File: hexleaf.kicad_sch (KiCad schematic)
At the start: 42 parts, among them IC1 ESP32-C3-FH4, J2 Conn_01x04, J5 Conn_01x08, J6 Conn_01x04, J7 Conn_01x08, SW1 SW_SPST, SW2 SW_SPST, Y1 ECS-400-10-37B2-CKM-TR

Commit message: added buck
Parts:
- added C? (x3): 22uF/16V, Resistor_SMD:R_0603_1608Metric, symbol Device:C_Small
- added C? (x2): 100n/50V, Resistor_SMD:R_0603_1608Metric, symbol Device:C_Small
- added L?: 33uH, hexleaf:CYH127, symbol Device:L_Small
- added R?: 24k, Resistor_SMD:R_0603_1608Metric, symbol Device:R_Small
- added R?: 75k, Resistor_SMD:R_0603_1608Metric, symbol Device:R_Small
- added R?: 100k, Resistor_SMD:R_0603_1608Metric, symbol Device:R_Small
- added R?: 0R, Resistor_SMD:R_0603_1608Metric, symbol Device:R_Small
- added U?: ZTP7193MA, Package_TO_SOT_SMD:SOT-23-8, symbol hexleaf:ZTP7193MA
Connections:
- net +3V3: now also C?.1, C?.1, L?.2, R?.2
- net GND: now also C?.2, C?.2, C?.2, C?.2, R?.1, U?.4 (GND)
- net VIN: now also C?.1, R?.1, U?.2 (VIN)
- new net: C?.1, L?.1, U?.3 (SW)
- new net: C?.2, U?.5 (BOOT)
- new net: R?.2, U?.6 (EN/SYNC)
- new net: C?.1, U?.7 (VCC)
- new net: R?.2, U?.8 (FB)
- new net: R?.1, R?.1, R?.2
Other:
- note added: "?"
- moved on the sheet: C1, C10, C2, C4, C5, C7, C9, L1

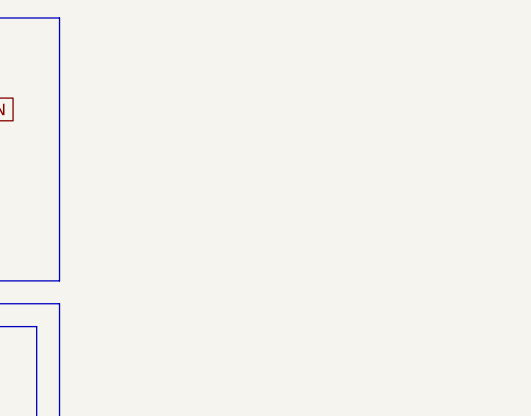
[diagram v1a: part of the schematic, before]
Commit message: added crystal
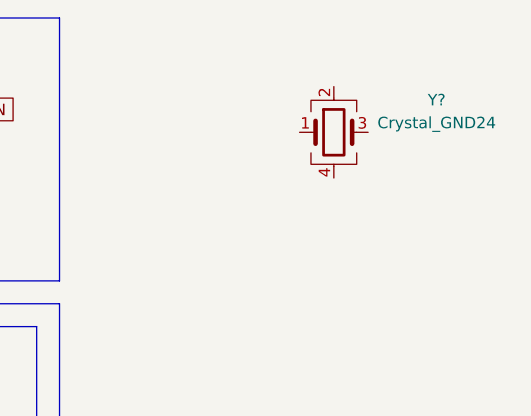
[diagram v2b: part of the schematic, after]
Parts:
- added Y?: Crystal_GND24, symbol Device:Crystal_GND24
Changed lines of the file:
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@@
     (pin "2")
+  )
+  (symbol (lib_id "Device:Crystal_GND24") (at 361.95 38.1 0) (unit 1)
+    (in_bom yes) (on_board yes) (fields_autoplaced)
+    (property "Reference" "Y?" (id 0) (at 373.38 34.5186 0))
+    (property "Value" "Crystal_GND24" (id 1) (at 373.38 37.0586 0))
+    (property "Footprint" "" (id 2) (at 361.95 38.1 0)
+      (effects (font (size 1.27 1.27)) hide)
+    )
+    (property "Datasheet" "~" (id 3) (at 361.95 38.1 0)
+      (effects (font (size 1.27 1.27)) hide)
+    )
+    (pin "1")
+    (pin "2")
+    (pin "3")
+    (pin "4")
   )
   (symbol (lib_id "hexleaf:ESP32-C3") (at 210.82 82.55 0) (unit 1)
@@
       (reference "Y1") (unit 1) (value "ECS-400-10-37B2-CKM-TR") (footprint "hexleaf:ECS4001037B2CKMTR")
     )
-  )
+    (path "/af67bf30-256d-4dee-a104-c380bafd6a33"
+      (reference "Y?") (unit 1) (value "Crystal_GND24") (footprint "")
+    )
+  )
